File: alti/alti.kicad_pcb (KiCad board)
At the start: 2 copper layers, 25 x 75 mm, 13 parts, among them J2 PINHD_1x2_Female, J3 10118193-0001LF, U1 ESP32-S3-WROOM-1-N8R8, U2 TLV75533PDYDR, U3 BMP384, U5 MPU-6500, U6 W25Q128JVSIQ

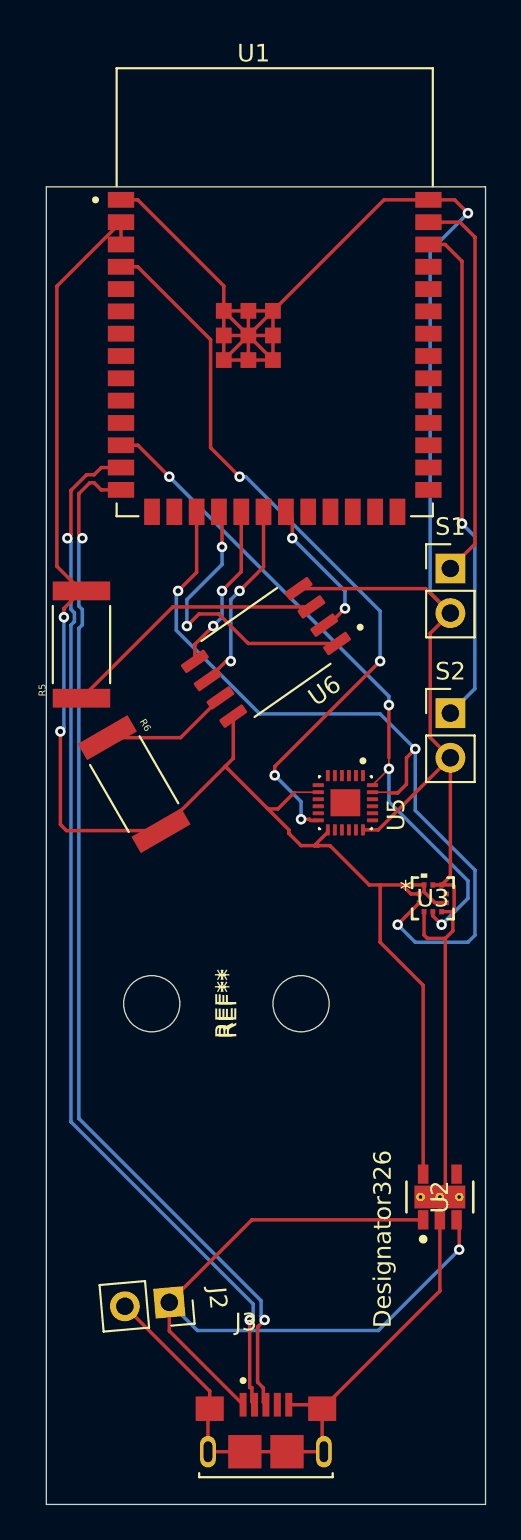
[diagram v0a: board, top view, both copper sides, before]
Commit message: update PCB based on feedback
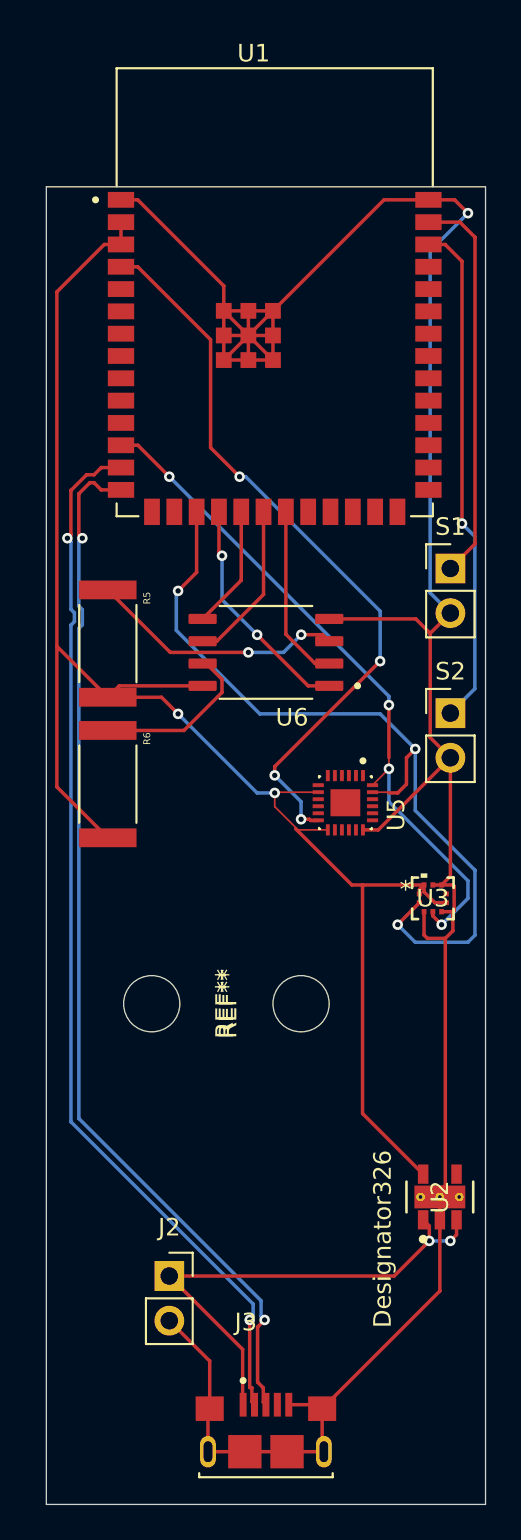
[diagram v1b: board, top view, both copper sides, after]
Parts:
- moved R5 1.50 mm to (93.5, 53.0), turned to -90 degrees
- moved J2 1.50 mm to (97.0, 89.0), turned to 0 degrees
- moved R6 1.50 mm to (93.5, 61.0), turned to -90 degrees
- turned U6 to 180 degrees
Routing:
- net VBUS: track 44.8 -> 28.6 mm, vias 1 -> 2
- net GND: track 162.5 -> 157.5 mm
- net 3V3: track 91.8 -> 95.7 mm
- net CS: track 16.9 -> 13.2 mm
- net MOSI: track 9.60 -> 7.01 mm, vias 2 -> 0
- net Net-(U6-/HOLD/RESET(IO3)): track 7.38 -> 9.62 mm
- net CLK: track 11.0 -> 9.27 mm, vias 2 -> 0
- net MISO: track 8.47 -> 10.1 mm, vias 2 -> 0
- net Net-(U6-/WP(IO2)): track 15.2 -> 14.6 mm, vias 0 -> 2
